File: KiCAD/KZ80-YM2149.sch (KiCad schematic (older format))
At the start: 55 parts, among them J1 Audio-Jack-3_2Switches, J2 ADDR JP, J3 JOYSTICK1, J4 SBC8080 BUS, J5 JOYSTICK2, J6 CMT IN, J7 SOUND-IN, U1 74HC138, U2 74HC00, U3 74HC02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

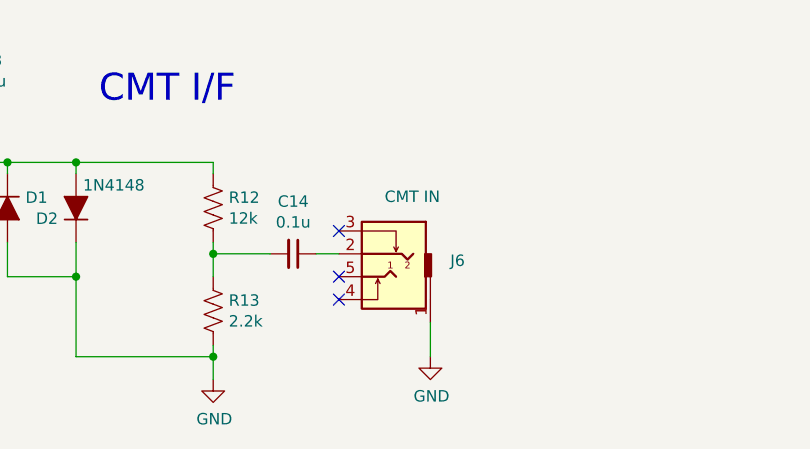
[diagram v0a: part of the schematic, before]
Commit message: 回路図間違い修正・ガーバー再出力
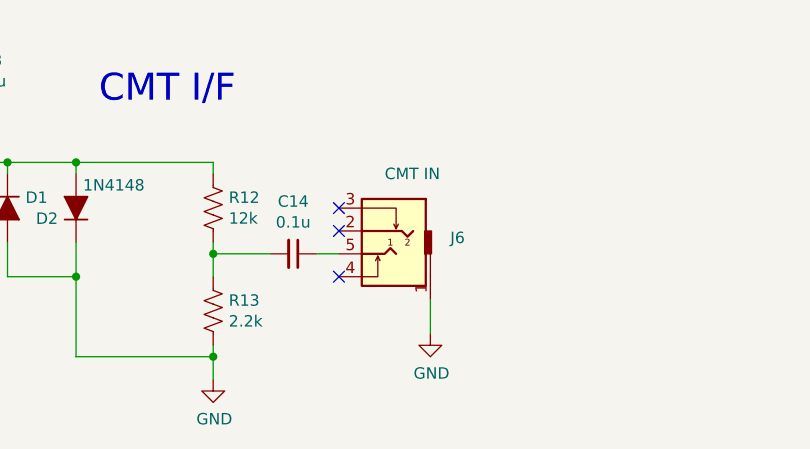
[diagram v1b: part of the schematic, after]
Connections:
- net at C14.1: now also J6.5; no longer J6.2
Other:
- moved on the sheet: J6
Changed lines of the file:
@@
 L power:GND #PWR038
 U 1 1 5F964BBF
-P 12050 9650
-F 0 "#PWR038" H 12050 9400 50  0001 C CNN
-F 1 "GND" H 12055 9477 50  0000 C CNN
-F 2 "" H 12050 9650 50  0001 C CNN
-F 3 "" H 12050 9650 50  0001 C CNN
-	1    12050 9650
+P 12050 9550
+F 0 "#PWR038" H 12050 9300 50  0001 C CNN
+F 1 "GND" H 12055 9377 50  0000 C CNN
+F 2 "" H 12050 9550 50  0001 C CNN
+F 3 "" H 12050 9550 50  0001 C CNN
+	1    12050 9550
 	1    0    0    -1
 $EndComp
 Wire Wire Line
-	12050 9500 12050 9650
+	12050 9400 12050 9550
 Wire Wire Line
 	8550 9600 8550 9700
@@
 L YM2151-rescue:Audio-Jack-3_2Switches J6
 U 1 1 60BA0AA3
-P 11850 9300
-F 0 "J6" H 11563 9370 50  0000 R CNN
-F 1 "CMT IN" H 11850 9650 50  0000 R CNN
-F 2 "AJ-1780:AJ-1780" H 12100 9400 50  0001 C CNN
-F 3 "" H 12100 9400 50  0001 C CNN
-	1    11850 9300
+P 11850 9200
+F 0 "J6" H 11563 9270 50  0000 R CNN
+F 1 "CMT IN" H 11850 9550 50  0000 R CNN
+F 2 "AJ-1780:AJ-1780" H 12100 9300 50  0001 C CNN
+F 3 "" H 12100 9300 50  0001 C CNN
+	1    11850 9200
 	-1   0    0    -1
 $EndComp
-NoConn ~ 11650 9100
+NoConn ~ 11650 9000
 NoConn ~ 11650 9300
-NoConn ~ 11650 9400
 Text Notes 10600 8550 0    118  ~ 0
 CMT I/F
@@
 Wire Wire Line
 	9750 1450 9750 1500
+NoConn ~ 11650 9100
 Wire Bus Line
 	4500 3550 4500 4500
